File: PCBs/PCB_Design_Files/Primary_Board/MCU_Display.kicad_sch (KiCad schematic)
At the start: 7 parts, among them U16 XIAO-ESP32-S3-SMD, U6 DM-OLED096-636

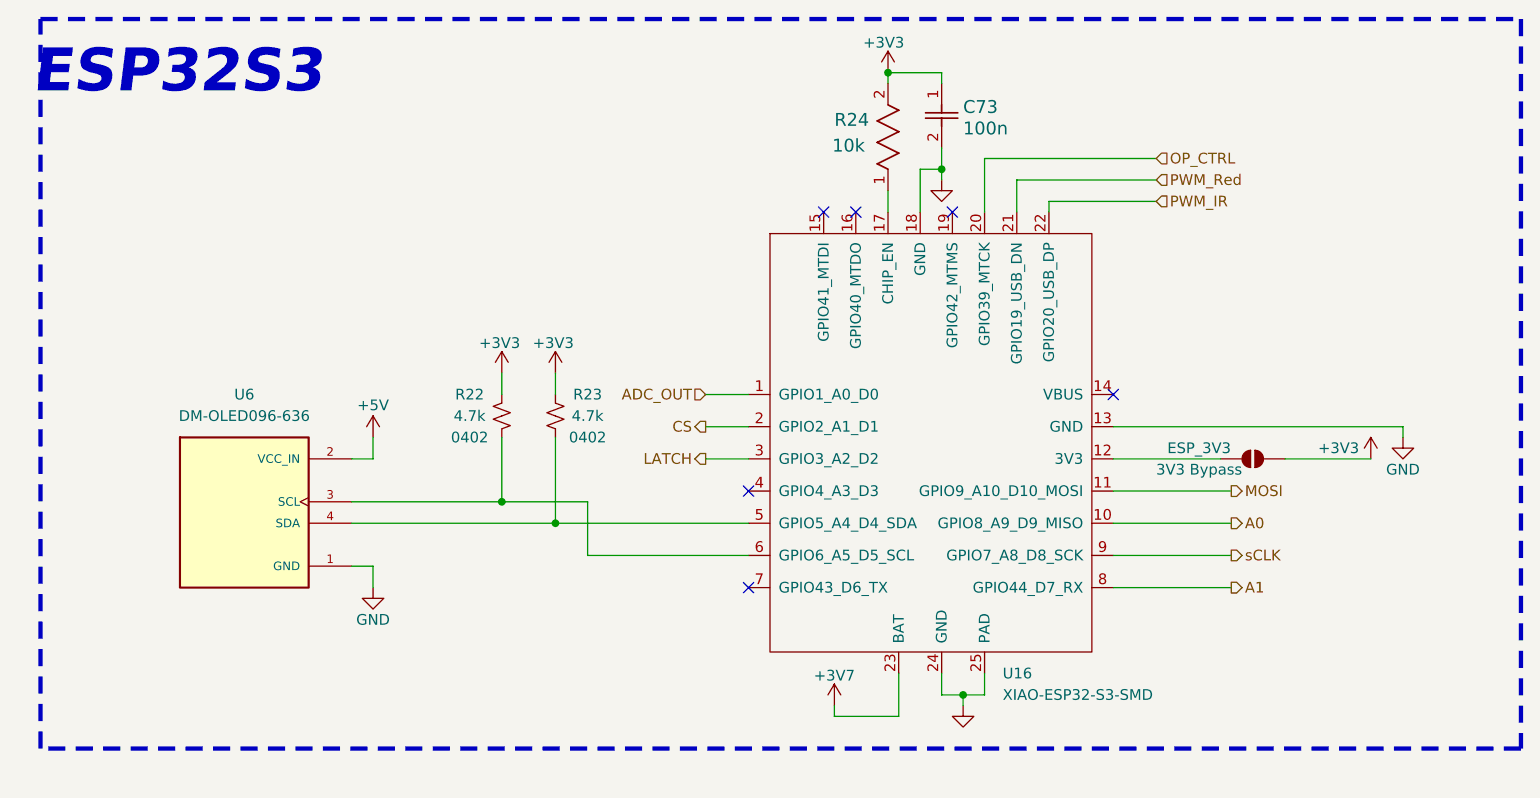
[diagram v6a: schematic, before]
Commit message: updated mcu connections, vbat divider to mcu
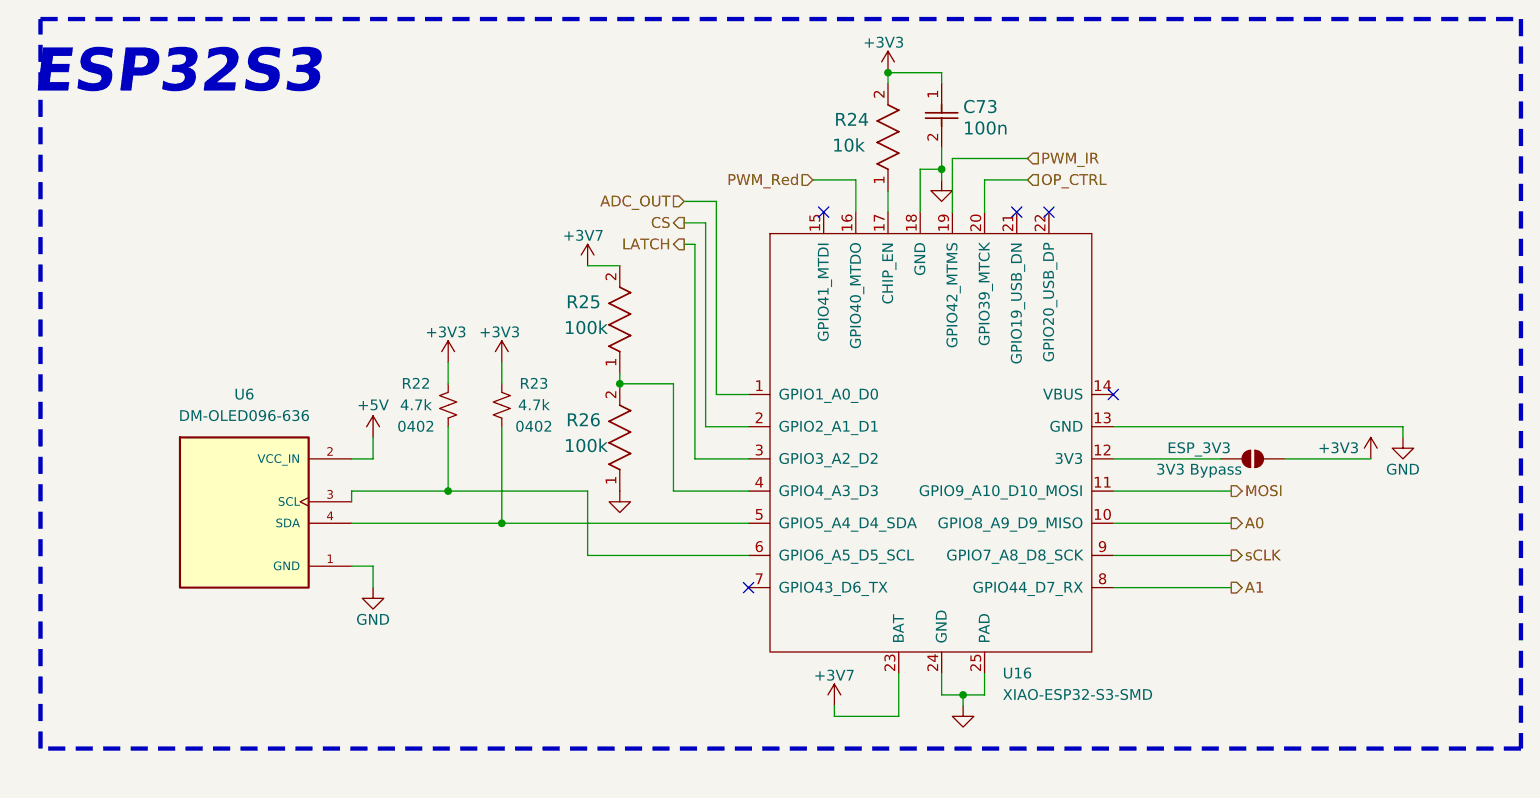
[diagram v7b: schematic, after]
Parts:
- added R25, R26: 100k, Project Footprints:0603_resistor, symbol project_symbols:0603_resistor
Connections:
- net +3V7: now also R25.2
- net GND: now also R26.1
- net PWM_IR: now also U16.19 (GPIO42_MTMS); no longer U16.22 (GPIO20_USB_DP)
- net PWM_Red: now also U16.16 (GPIO40_MTDO); no longer U16.21 (GPIO19_USB_DN)
- net at U16.4 (GPIO4_A3_D3): now also R25.1, R26.2
- no-connect marks 6 -> 5
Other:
- moved on the sheet: R22, R23

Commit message: 3.3V gpio
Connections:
- net +3V3: now also U16.7 (GPIO43_D6_TX)
- no-connect marks 5 -> 4
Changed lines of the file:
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@@
-	)
-	(no_connect
-		(at 101.6 83.82)
 	)
 	(no_connect
@@
 	(wire
 		(pts
+			(xy 78.74 83.82) (xy 78.74 90.17)
+		)
+		(stroke
+			(width 0)
+			(type default)
+		)
+	)
+	(wire
+		(pts
 			(xy 72.39 64.77) (xy 72.39 76.2)
 		)
@@
 	(wire
 		(pts
+			(xy 78.74 90.17) (xy 91.44 90.17)
+		)
+		(stroke
+			(width 0)
+			(type default)
+		)
+	)
+	(wire
+		(pts
 			(xy 72.39 57.15) (xy 72.39 59.69)
 		)
@@
 	(wire
 		(pts
+			(xy 91.44 83.82) (xy 91.44 90.17)
+		)
+		(stroke
+			(width 0)
+			(type default)
+		)
+	)
+	(wire
+		(pts
 			(xy 66.04 72.39) (xy 82.55 72.39)
 		)
@@
 		(pts
 			(xy 93.98 40.64) (xy 96.52 40.64)
+		)
+		(stroke
+			(width 0)
+			(type default)
+		)
+	)
+	(wire
+		(pts
+			(xy 101.6 83.82) (xy 91.44 83.82)
 		)
 		(stroke
@@
 					(unit 1)
 				)
+			)
+		)
+	)
+	(symbol
+		(lib_id "power:+3V3")
+		(at 78.74 83.82 0)
+		(unit 1)
+		(exclude_from_sim no)
+		(in_bom yes)
+		(on_board yes)
+		(dnp no)
+		(property "Reference" "#PWR024"
+			(at 78.74 87.63 0)
+			(effects
+				(font
+					(size 1.27 1.27)
+				)
+				(hide yes)
+			)
+		)
+		(property "Value" "+3V3"
+			(at 74.93 82.55 0)
+			(effects
+				(font
+					(size 1.27 1.27)
+				)
+			)
+		)
+		(property "Footprint" ""
+			(at 78.74 83.82 0)
+			(effects
+				(font
+					(size 1.27 1.27)
+				)
+				(hide yes)
+			)
+		)
+		(property "Datasheet" ""
+			(at 78.74 83.82 0)
+			(effects
+				(font
+					(size 1.27 1.27)
+				)
+				(hide yes)
+			)
+		)
+		(property "Description" "Power symbol creates a global label with name \"+3V3\""
+			(at 78.74 83.82 0)
+			(effects
+				(font
+					(size 1.27 1.27)
+				)
+				(hide yes)
+			)
+		)
+		(pin "1"
+		)
+		(instances
+			(project "Primary_Board"
+				(path "/8c3d01e8-a984-4e4e-9220-7d351336a99b/c9d7a52b-c624-454d-af83-5076e9ccc3d1"
+					(reference "#PWR024")
+					(unit 1)
+				)
